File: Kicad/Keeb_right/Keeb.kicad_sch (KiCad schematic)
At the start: 23 parts, among them J1 MJ-4PP-9, SW1 CherryMX, SW10 CherryMX, SW11 CherryMX, SW12 CherryMX, SW13 CherryMX, SW14 CherryMX, SW15 CherryMX, SW16 CherryMX, SW17 CherryMX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

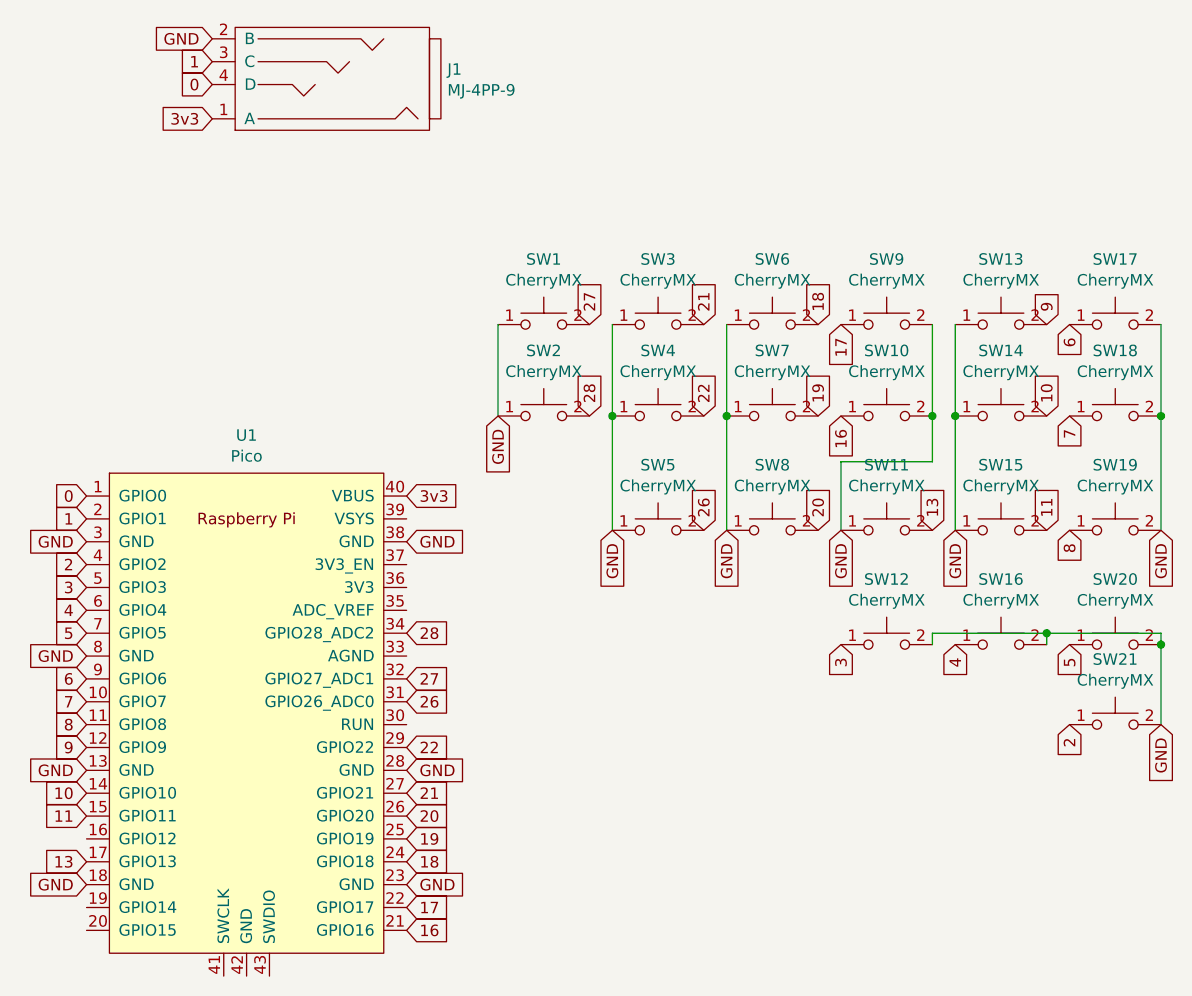
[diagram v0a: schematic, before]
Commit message: Sorted things into folders, finisher right and left halves
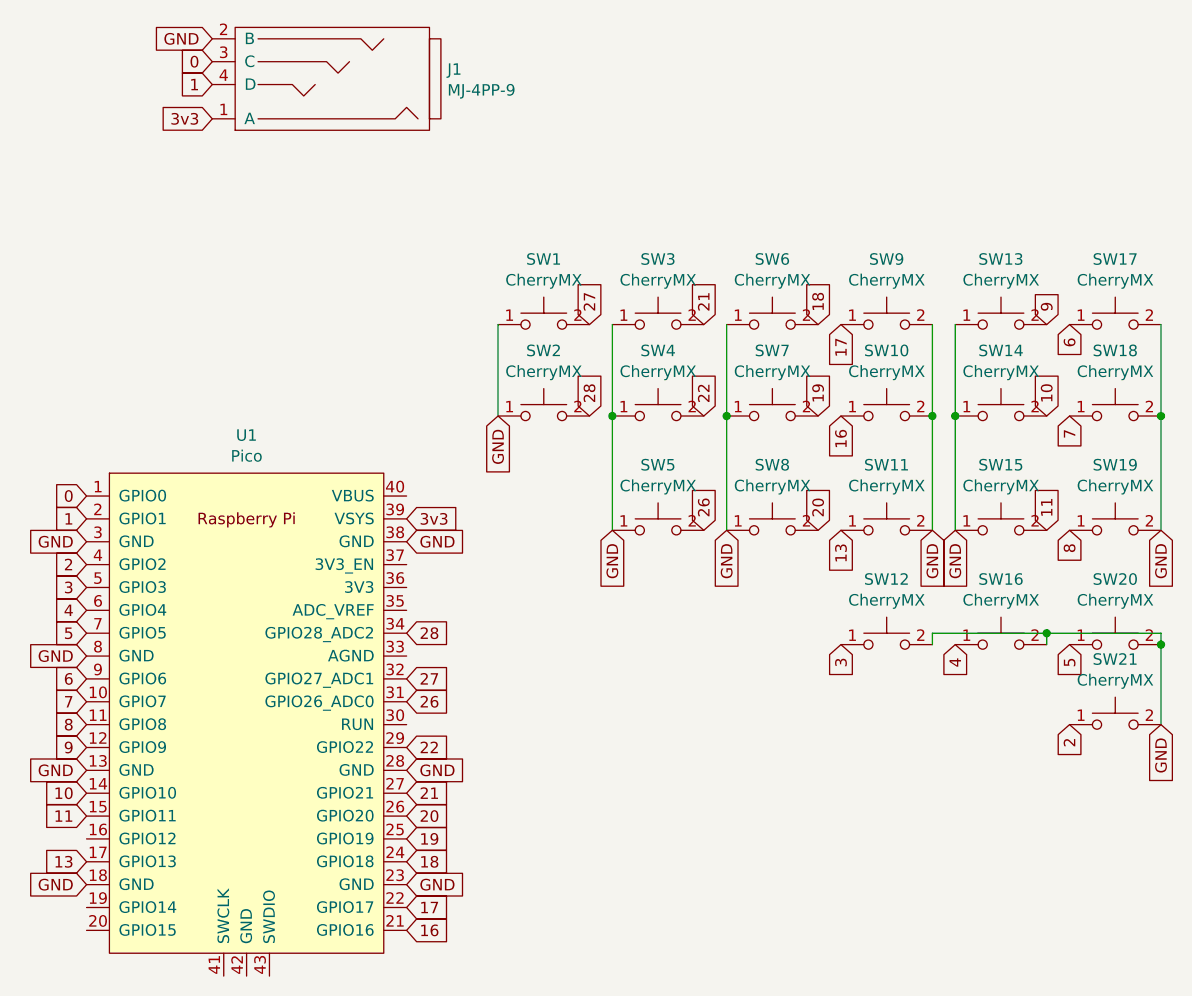
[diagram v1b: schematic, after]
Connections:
- net 0: now also J1.3 (C); no longer J1.4 (D)
- net 1: now also J1.4 (D); no longer J1.3 (C)
- net 13: now also SW11.1; no longer SW11.2
- net 3v3: now also U1.39 (VSYS); no longer U1.40 (VBUS)
- net GND: now also SW11.2; no longer SW11.1
